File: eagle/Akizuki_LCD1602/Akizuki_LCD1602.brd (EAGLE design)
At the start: 93.7 x 71.1 mm, 4 parts

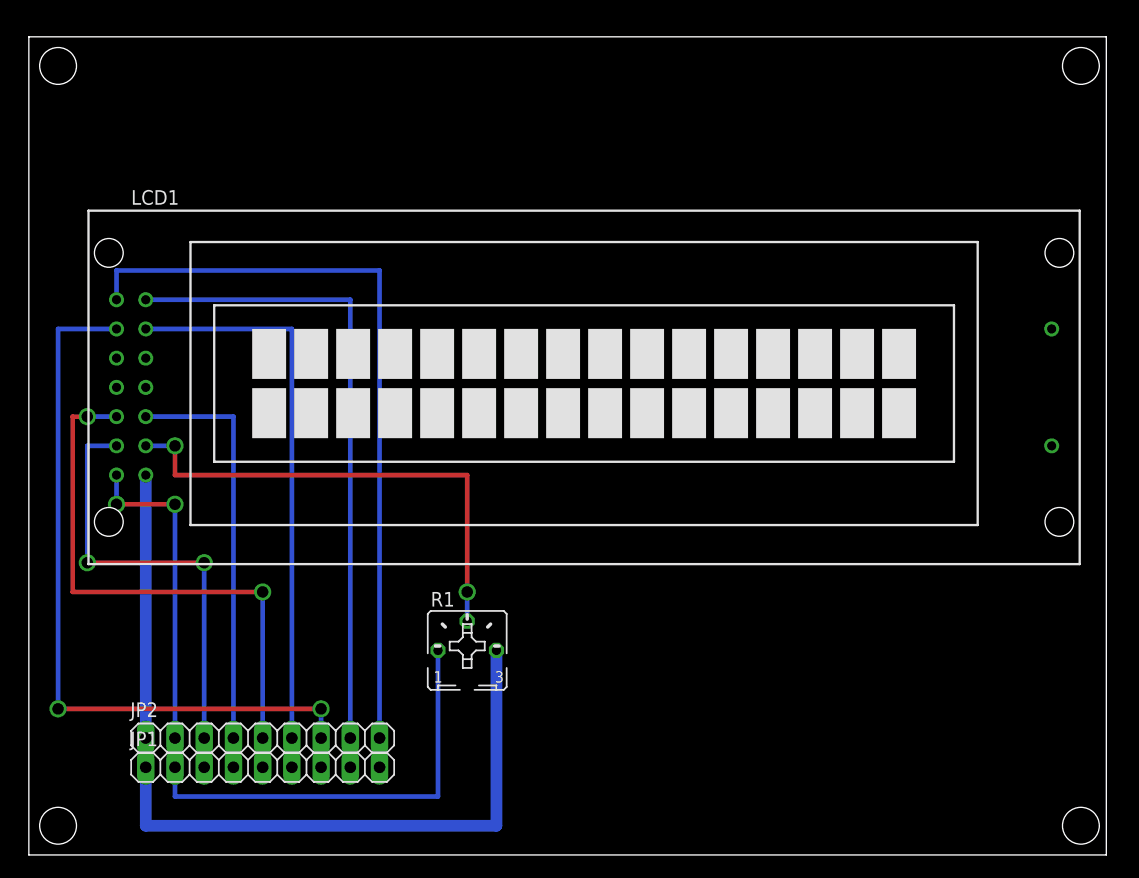
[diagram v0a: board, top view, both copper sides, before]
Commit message: ジュンフロン線のジャンパで配線
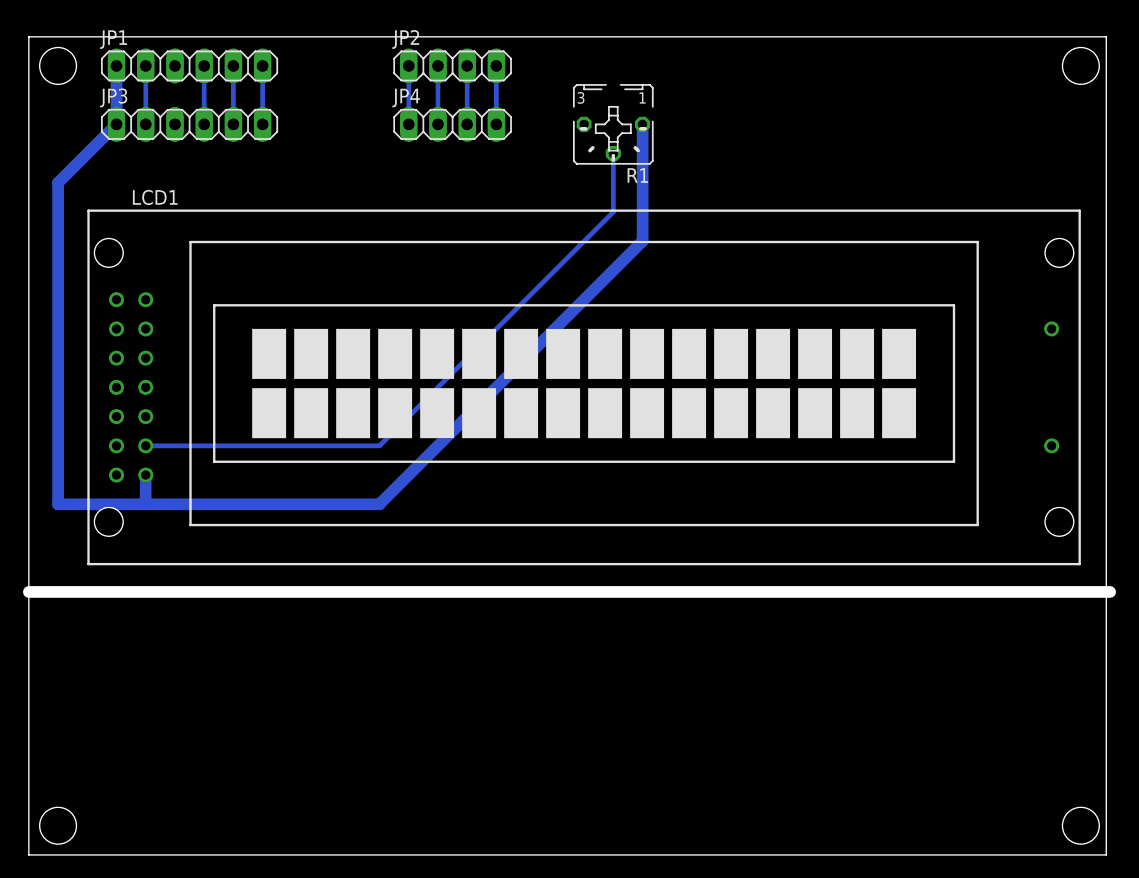
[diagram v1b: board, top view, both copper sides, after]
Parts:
- added JP3: (no value), pinhead:1X06
- added JP4: (no value), pinhead:1X04
- JP1: value IN1 -> (none); device pinhead:1X09 -> pinhead:1X06
- JP2: value IN2 -> (none); device pinhead:1X09 -> pinhead:1X04
- moved JP1 61.3 mm to (14.0, 68.6)
- moved JP2 60.7 mm to (36.8, 68.6)
- moved R1 47.5 mm to (50.8, 63.5), turned to 180 degrees
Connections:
- net +5V: now also JP1.2, JP3.2, LCD1.P$2; no longer JP1.1, JP2.1, LCD1.P$1
- net GND: now also JP1.1, JP3.1, LCD1.P$1; no longer JP1.2, JP2.2, LCD1.P$2
- net N$11: now also JP2.4, JP4.4; no longer JP1.9, JP2.9
- net N$2: now also JP1.4, JP3.4; no longer JP1.3, JP2.3
- net N$3: now also JP1.5, JP3.5; no longer JP1.4, JP2.4
- net N$4: now also JP1.6, JP3.6; no longer JP1.5, JP2.5
- net N$5: now also JP2.1, JP4.1; no longer JP1.6, JP2.6
- net N$6: now also JP2.2, JP4.2; no longer JP1.7, JP2.7
- net N$7: now also JP2.3, JP4.3; no longer JP1.8, JP2.8
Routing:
- net +5V: track 76.2 -> 5.08 mm
- net N$11: track 68.6 -> 5.08 mm
- net N$6: track 66.0 -> 5.08 mm, vias 2 -> 0
- net N$7: track 58.4 -> 5.08 mm
- net N$5: track 50.8 -> 5.08 mm
- net N$4: track 50.8 -> 5.08 mm, vias 2 -> 0
- net GND: track 68.6 -> 113.2 mm, vias 2 -> 0
- net N$2: track 40.6 -> 5.08 mm, vias 2 -> 0
- net N$3: track 38.1 -> 5.08 mm
- net N$1: track 43.2 -> 54.1 mm, vias 2 -> 0
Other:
- board size 93.7 x 71.1 mm -> 94 x 71.1 mm
- board text added: "Cut Off"

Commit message: Debug
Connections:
- net +5V: now also LCD1.P$1; no longer LCD1.P$2
- net GND: now also LCD1.P$2; no longer LCD1.P$1
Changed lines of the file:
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@@
 <signals>
 <signal name="GND">
-<contactref element="LCD1" pad="P$1"/>
 <contactref element="R1" pad="A"/>
 <contactref element="JP1" pad="1"/>
@@
 <wire x1="53.34" y1="53.34" x2="30.48" y2="30.48" width="1.016" layer="16"/>
 <wire x1="7.62" y1="68.58" x2="7.62" y2="63.5" width="1.016" layer="16"/>
-<wire x1="30.48" y1="30.48" x2="10.16" y2="30.48" width="1.016" layer="16"/>
-<wire x1="10.16" y1="30.48" x2="2.54" y2="30.48" width="1.016" layer="16"/>
+<wire x1="30.48" y1="30.48" x2="7.62" y2="30.48" width="1.016" layer="16"/>
+<wire x1="7.62" y1="30.48" x2="2.54" y2="30.48" width="1.016" layer="16"/>
 <wire x1="2.54" y1="30.48" x2="2.54" y2="58.42" width="1.016" layer="16"/>
-<wire x1="10.16" y1="33.02" x2="10.16" y2="30.48" width="1.016" layer="16"/>
 <wire x1="7.62" y1="63.5" x2="2.54" y2="58.42" width="1.016" layer="16"/>
+<contactref element="LCD1" pad="P$2"/>
+<wire x1="7.62" y1="33.02" x2="7.62" y2="30.48" width="1.016" layer="16"/>
 </signal>
 <signal name="+5V">
-<contactref element="LCD1" pad="P$2"/>
 <contactref element="R1" pad="E"/>
 <contactref element="JP1" pad="2"/>
 <contactref element="JP3" pad="2"/>
 <wire x1="10.16" y1="68.58" x2="10.16" y2="63.5" width="0.4064" layer="16"/>
+<contactref element="LCD1" pad="P$1"/>
 <wire x1="10.16" y1="63.5" x2="48.26" y2="63.5" width="0" layer="19" extent="1-1"/>
-<wire x1="7.62" y1="33.02" x2="10.16" y2="63.5" width="0" layer="19" extent="1-1"/>
+<wire x1="10.16" y1="33.02" x2="10.16" y2="63.5" width="0" layer="19" extent="1-1"/>
 </signal>
 <signal name="N$1">
